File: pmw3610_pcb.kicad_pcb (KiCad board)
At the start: 2 copper layers, 15.4 x 29.9 mm, 15 parts, among them J1 Conn_01x02, J2 Conn_01x04, U1 PMW3610, U2 TLV74318PDBVR

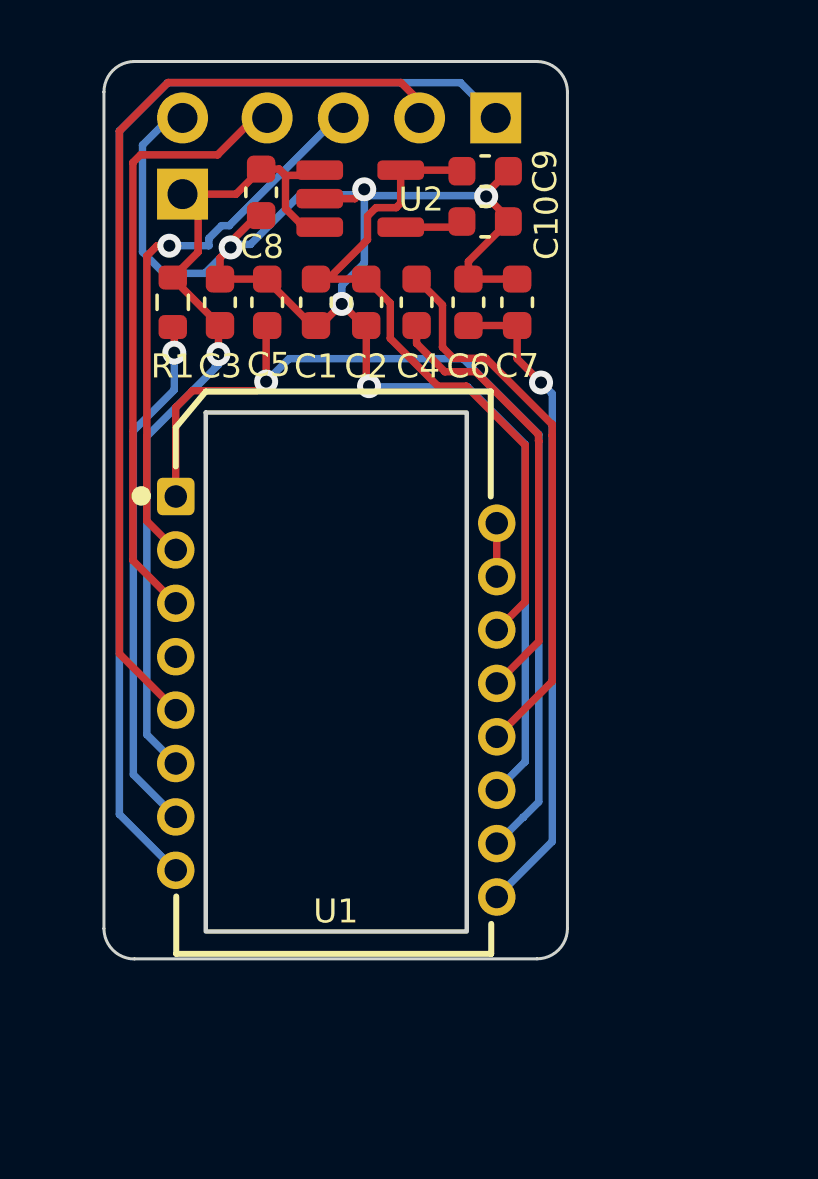
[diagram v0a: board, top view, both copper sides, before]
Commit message: modify size (25mm x 22mm)
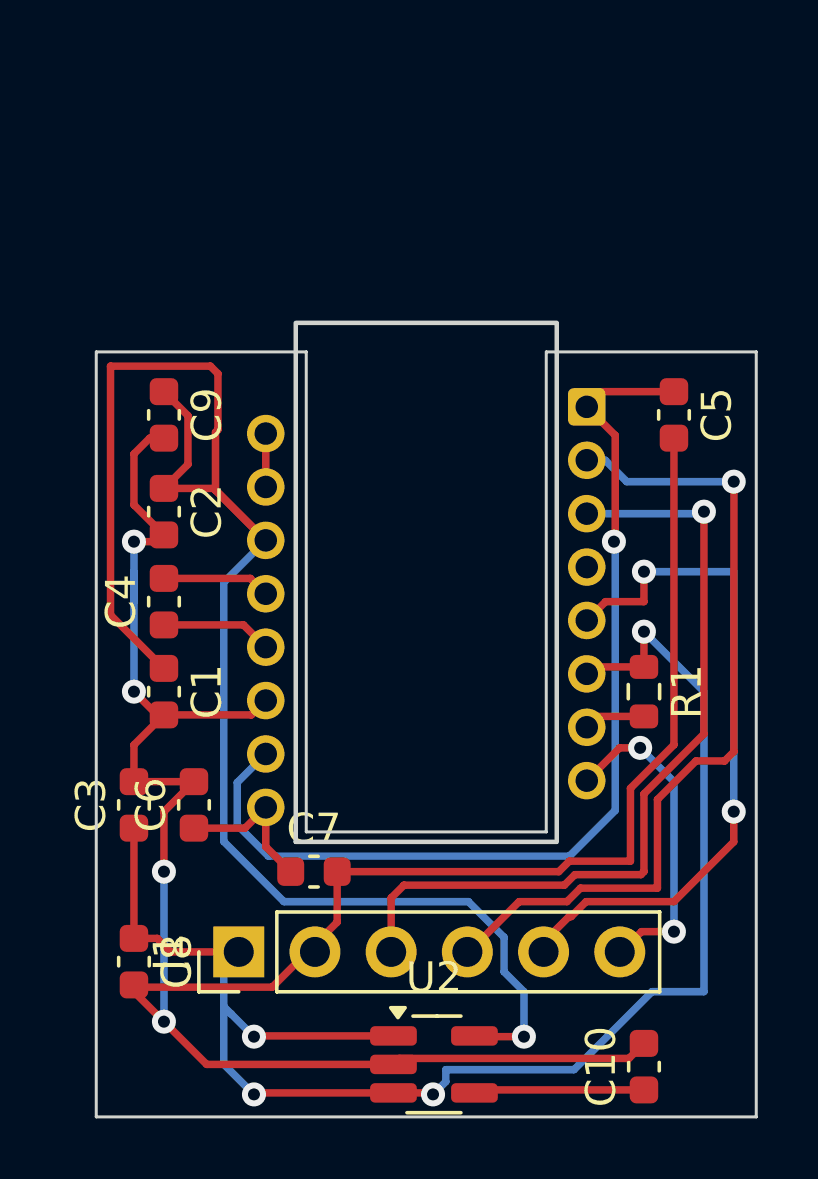
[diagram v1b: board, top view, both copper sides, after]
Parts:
- removed J2: Conn_01x04, Connector_PinHeader_2.54mm:PinHeader_1x04_P2.54mm_Vertical
- removed U1: PMW3610, pmw3610_pcb:PMW3610DM-SUDU 16Pin
- added U4: PMW3610, pmw3610_pcb:PMW3610DM-SUDU 16Pin, B.Cu at (153.0, 100.0)
- J1: value Conn_01x02 -> Conn_01x06; footprint Connector_PinHeader_2.54mm:PinHeader_1x02_P2.54mm_Vertical -> Connector_PinHeader_2.54mm:PinHeader_1x06_P2.54mm_Vertical
- moved U2 29.0 mm to (153.3, 115.8)
- moved C10 28.7 mm to (160.3, 115.8), turned to 90 degrees
- moved C8 26.0 mm to (143.3, 112.3)
- moved J1 25.3 mm to (146.8, 112.0), turned to 90 degrees
- moved R1 20.4 mm to (160.3, 103.3)
- moved C7 20.2 mm to (149.3, 109.3), turned to 0 degrees
- moved C6 19.1 mm to (145.3, 107.1)
- moved C3 17.0 mm to (143.3, 107.1)
- moved C5 14.1 mm to (161.3, 94.1), turned to -90 degrees
- moved C1 13.9 mm to (144.3, 103.3)
- moved C9 13.4 mm to (144.3, 94.1), turned to -90 degrees
- moved C4 13.1 mm to (144.3, 100.3), turned to 90 degrees
- moved C2 9.71 mm to (144.3, 97.3)
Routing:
- net +1V8: track 23.5 -> 55.3 mm, vias 0 -> 1
- net MOTION: track 39.4 -> 10.9 mm, vias 0 -> 2
- net GND: track 59.9 -> 82.9 mm, vias 5 -> 4
- net VIN: track 30.0 -> 51.1 mm, vias 1 -> 4
- net Net-(U4-VCP): track 22.6 -> 5.17 mm, vias 1 -> 0
- net Net-(U4-NRESET): track 17.5 -> 2.06 mm, vias 1 -> 0
- net Net-(U4-CP): track 18.5 -> 3.70 mm
- net Net-(U4-CN): track 14.8 -> 3.61 mm
- net SDIO: track 18.4 -> 27.5 mm
- net nCS: track 31.0 -> 23.2 mm, vias 0 -> 2
- net SCLK: track 20.6 -> 27.4 mm, vias 0 -> 1
- net Net-(U2-NC): track 2.12 -> 5.69 mm
- net Net-(U4--VCSEL): track 0.00 -> 1.78 mm
- net Net-(U1--VCSEL): track 1.78 -> 0.00 mm
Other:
- board size 15.4 x 29.9 mm -> 22 x 25.5 mm
- board text removed: "3v3"
- board text removed: "G"
- board text removed: "MOT CS DIO CLK"

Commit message: [jlcpcb] Add order files
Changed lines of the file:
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@@
 			(plot_on_all_layers_selection 0x0000000_00000000)
 			(disableapertmacros no)
-			(usegerberextensions no)
+			(usegerberextensions yes)
 			(usegerberattributes yes)
 			(usegerberadvancedattributes yes)
@@
 			(outputformat 1)
 			(mirror no)
-			(drillshape 1)
+			(drillshape 0)
 			(scaleselection 1)
-			(outputdirectory "")
+			(outputdirectory "./jlcpcb")
 		)
 	)
@@
 		(tags "capacitor")
 		(property "Reference" "C7"
-			(at 0 -1.43 360)
+			(at 0 -1.43 0)
 			(layer "F.SilkS")
 			(effects
@@
 		)
 		(property "Value" "10nF X7R"
-			(at 0 1.43 360)
+			(at 0 1.43 0)
 			(layer "F.Fab")
 			(effects
@@
 		)
 		(fp_text user "${REFERENCE}"
-			(at 0 0 360)
+			(at 0 0 0)
 			(layer "F.Fab")
 			(effects
@@
 		(sheetname "ルート")
 		(sheetfile "pmw3610_pcb.kicad_sch")
-		(attr through_hole)
+		(attr through_hole exclude_from_pos_files exclude_from_bom dnp)
 		(fp_line
 			(start -1.33 -1.33)
@@
 		(tags "SOT-23-5 hand-soldering")
 		(property "Reference" "U2"
-			(at 0 -2.9 360)
+			(at 0 -2.9 0)
 			(layer "F.SilkS")
 			(effects
@@
 		)
 		(property "Value" "TLV74318PDBVR"
-			(at 0 2.9 360)
+			(at 0 2.9 0)
 			(layer "F.Fab")
 			(effects
@@
 		(descr "PMW3610DM-SUDU special 16pin molded lead-frame DIP")
 		(property "Reference" "U4"
-			(at -10 0.5 0)
+			(at -10 0 0)
 			(layer "B.SilkS")
 			(effects
@@
 		)
 		(property "Value" "PMW3610"
-			(at 0 0 90)
+			(at 0 0 -90)
 			(layer "B.Fab")
 			(effects
@@
 		)
 		(property "Footprint" "pmw3610_pcb:PMW3610DM-SUDU 16Pin"
-			(at 0 0 90)
+			(at 0 0 -90)
 			(layer "B.Fab")
 			(hide yes)
@@
 		)
 		(property "Datasheet" ""
-			(at 0 0 90)
+			(at 0 0 -90)
 			(layer "B.Fab")
 			(hide yes)
@@
 		)
 		(property "Description" "Optical mouse sensor"
-			(at 0 0 90)
+			(at 0 0 -90)
 			(layer "B.Fab")
 			(hide yes)
@@
 		)
 		(fp_rect
-			(start -8.332 -4.35)
-			(end 8.968 4.35)
-			(stroke
-				(width 0.15)
-				(type solid)
-			)
-			(fill none)
-			(layer "Edge.Cuts")
-		)
-		(fp_rect
 			(start 10 6.5)
 			(end -9.5 -6.5)
@@
 			(pintype "input")
 		)
-		(zone
-			(net 0)
-			(net_name "")
-			(layers "*.Cu" "B.CrtYd")
-			(hatch edge 0.508)
-			(connect_pads
-				(clearance 0)
-			)
-			(min_thickness 0.254)
-			(filled_areas_thickness no)
-			(keepout
-				(tracks not_allowed)
-				(vias not_allowed)
-				(pads not_allowed)
-				(copperpour not_allowed)
-				(footprints not_allowed)
-			)
-			(fill
-				(thermal_gap 0.508)
-				(thermal_bridge_width 0.508)
-			)
-			(polygon
-				(pts
-					(xy 157.3688 108.3312) (xy 157.318 91.0084) (xy 148.6312 91.0084) (xy 148.6312 108.3312)
-				)
-			)
-		)
 		(group ""
-			(members "0051ebb1-42cc-4309-9bad-c2612f38a0aa" "42b1f514-efd4-4784-8a2b-5c74f047583c"
-				"7754271e-579a-4189-86de-500981ede4c1"
+			(members "5c1f305b-287b-4cf9-967a-f083a251786b" "660085b1-9296-4d97-b01d-bc9d5e91b58d"
+				"b0fccbf4-3394-4a3d-adb7-227343ebbd65"
 			)
 		)
